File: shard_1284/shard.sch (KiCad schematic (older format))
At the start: 4 parts, among them J0 Shard, J1 ISP, U1 ATmega1284P-MU

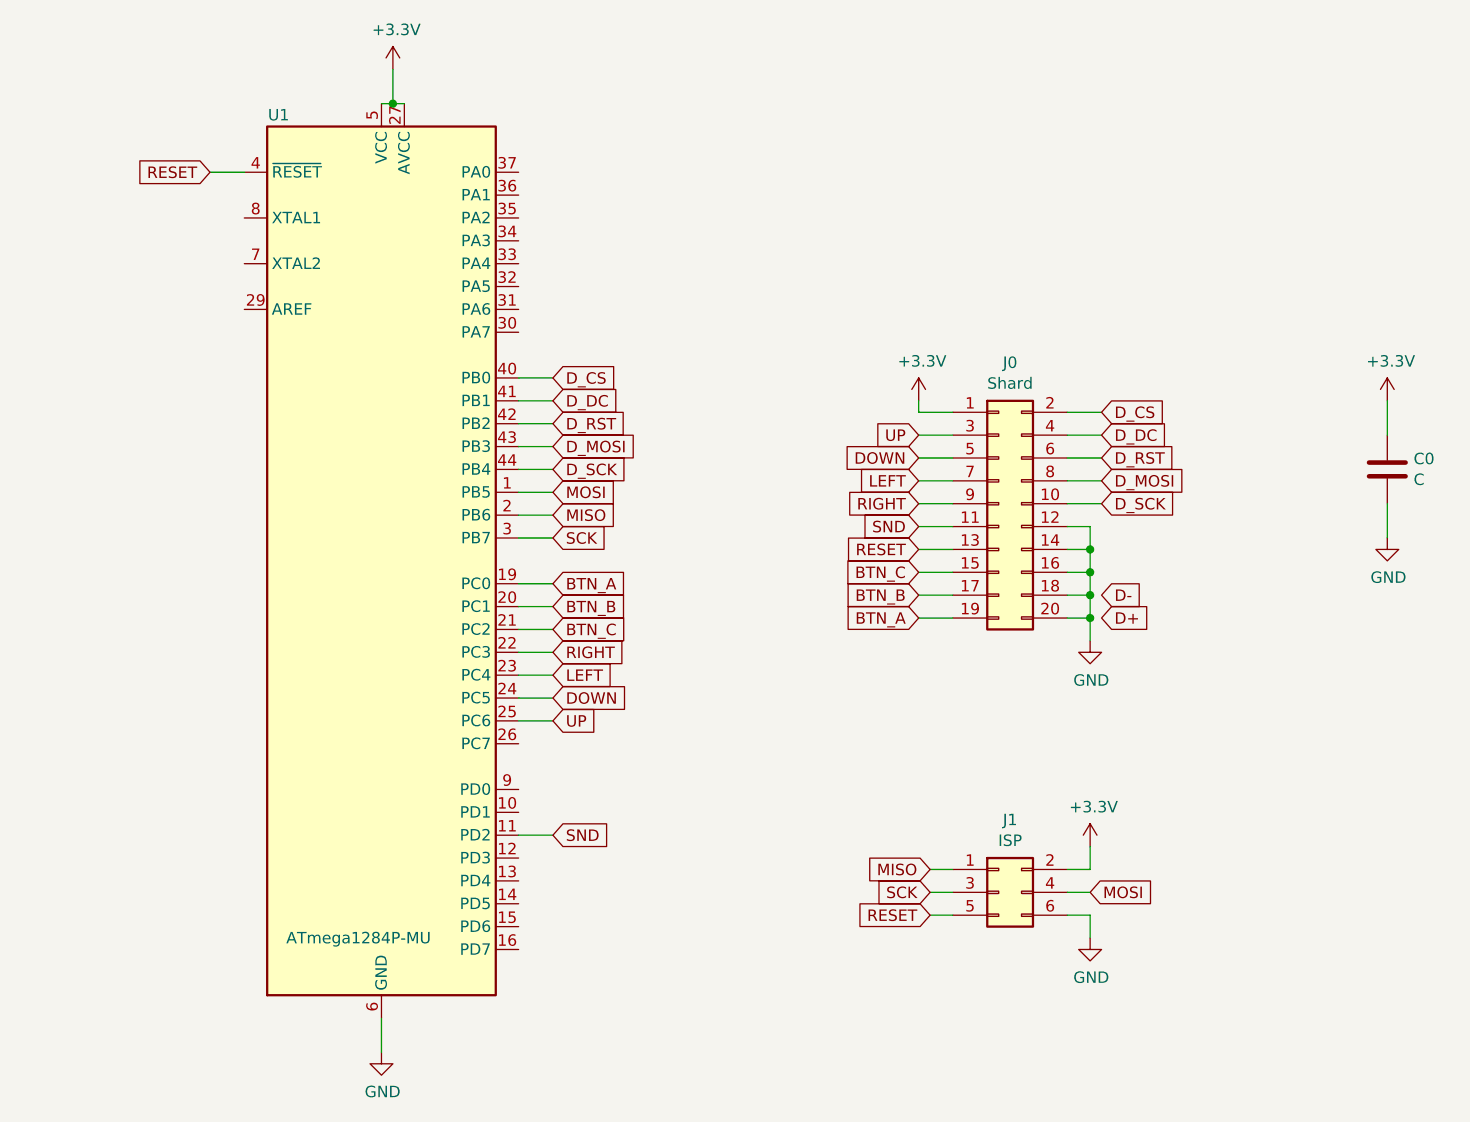
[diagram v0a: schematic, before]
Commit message: flip connector
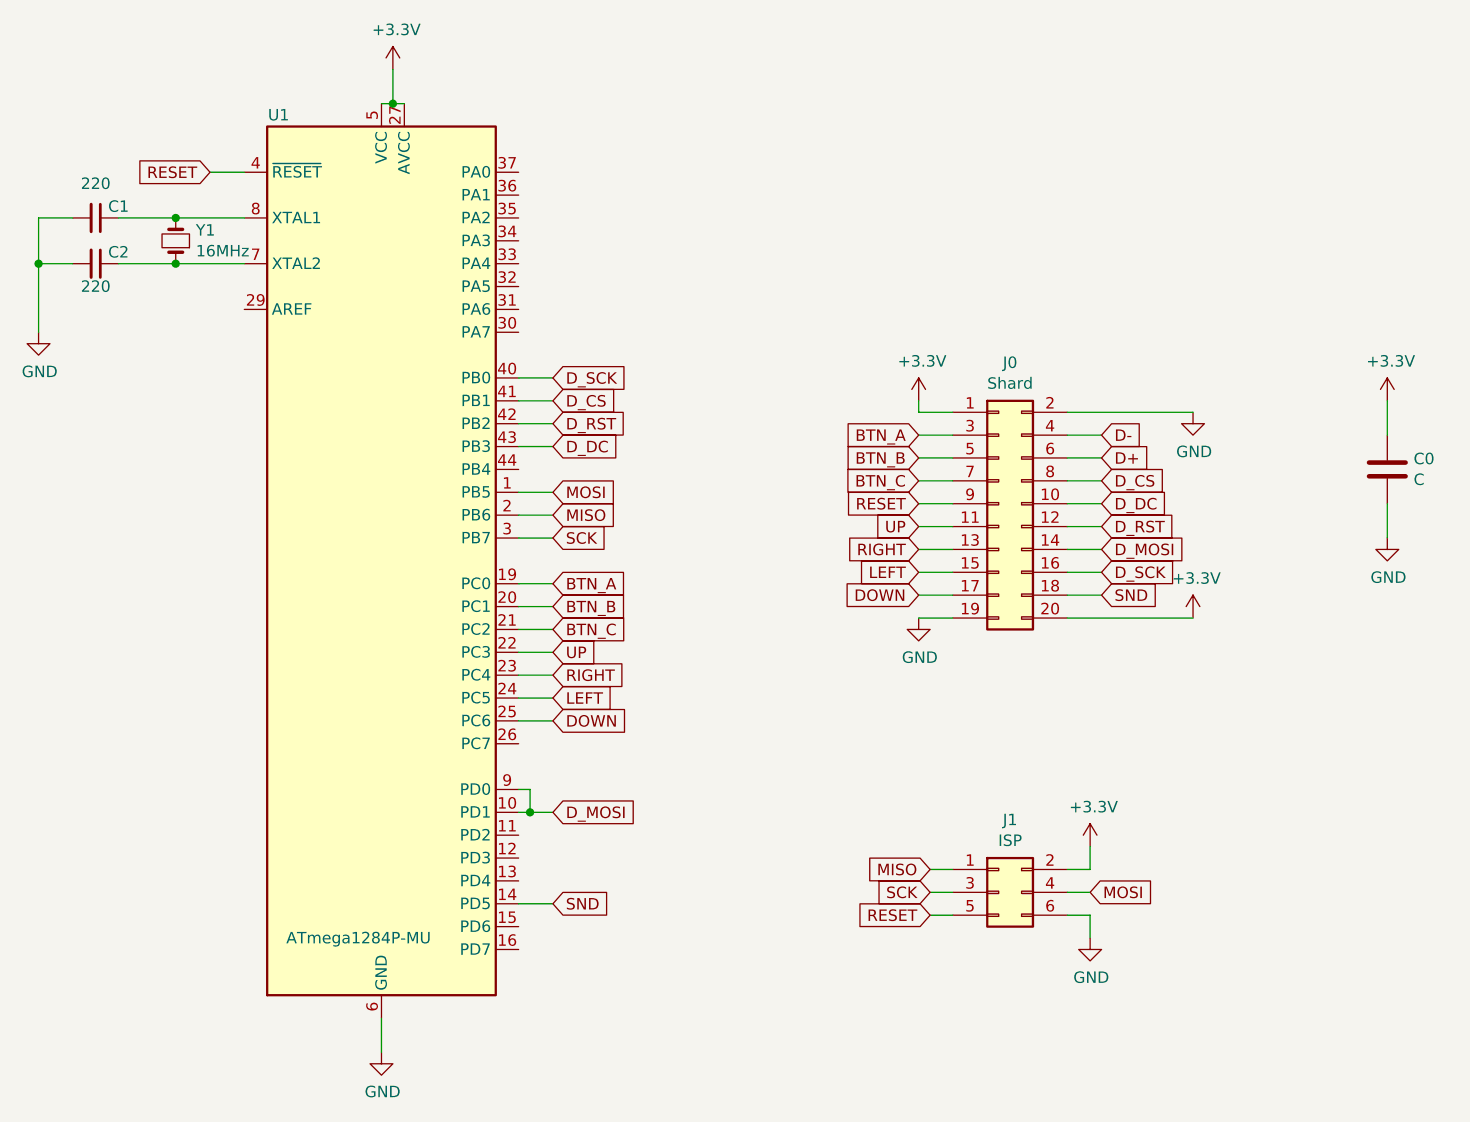
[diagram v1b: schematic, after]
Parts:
- added C1, C2: 220, Capacitor_THT:C_Rect_L7.0mm_W2.5mm_P5.00mm, symbol Device:C_Small
- added Y1: 16MHz, Crystal:Resonator-2Pin_W10.0mm_H5.0mm, symbol Device:Crystal_Small
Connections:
- net +3V3: now also J0.20 (Pin_20)
- net BTN_A: now also J0.3 (Pin_3); no longer J0.19 (Pin_19)
- net BTN_B: now also J0.5 (Pin_5); no longer J0.17 (Pin_17)
- net BTN_C: now also J0.7 (Pin_7); no longer J0.15 (Pin_15)
- net D+: now also J0.6 (Pin_6)
- net D-: now also J0.4 (Pin_4)
- net DOWN: now also J0.17 (Pin_17), U1.25 (PC6); no longer J0.5 (Pin_5), U1.24 (PC5)
- net D_CS: now also J0.8 (Pin_8), U1.41 (PB1); no longer J0.2 (Pin_2), U1.40 (PB0)
- net D_DC: now also J0.10 (Pin_10), U1.43 (PB3); no longer J0.4 (Pin_4), U1.41 (PB1)
- net D_MOSI: now also J0.14 (Pin_14), U1.10 (PD1), U1.9 (PD0); no longer J0.8 (Pin_8), U1.43 (PB3)
- net D_RST: now also J0.12 (Pin_12); no longer J0.6 (Pin_6)
- net D_SCK: now also J0.16 (Pin_16), U1.40 (PB0); no longer J0.10 (Pin_10), U1.44 (PB4)
- net GND: now also J0.19 (Pin_19), J0.2 (Pin_2), C1.2, C2.2; no longer J0.12 (Pin_12), J0.14 (Pin_14), J0.16 (Pin_16), J0.18 (Pin_18), J0.20 (Pin_20)
- net LEFT: now also J0.15 (Pin_15), U1.24 (PC5); no longer J0.7 (Pin_7), U1.23 (PC4)
- net RESET: now also J0.9 (Pin_9); no longer J0.13 (Pin_13)
- net RIGHT: now also J0.13 (Pin_13), U1.23 (PC4); no longer J0.9 (Pin_9), U1.22 (PC3)
- net SND: now also J0.18 (Pin_18), U1.14 (PD5); no longer J0.11 (Pin_11), U1.11 (PD2)
- net UP: now also J0.11 (Pin_11), U1.22 (PC3); no longer J0.3 (Pin_3), U1.25 (PC6)
- net at U1.7 (XTAL2): now also C2.1, Y1.1
- net at U1.8 (XTAL1): now also C1.1, Y1.2
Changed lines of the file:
@@
 L power:GND #PWR0102
 U 1 1 5BE69B29
-P 6500 3800
-F 0 "#PWR0102" H 6500 3550 50  0001 C CNN
-F 1 "GND" H 6505 3627 50  0000 C CNN
-F 2 "" H 6500 3800 50  0001 C CNN
-F 3 "" H 6500 3800 50  0001 C CNN
-	1    6500 3800
+P 5750 3700
+F 0 "#PWR0102" H 5750 3450 50  0001 C CNN
+F 1 "GND" H 5755 3527 50  0000 C CNN
+F 2 "" H 5750 3700 50  0001 C CNN
+F 3 "" H 5750 3700 50  0001 C CNN
+	1    5750 3700
 	1    0    0    -1
 $EndComp
@@
 $EndComp
 Wire Wire Line
-	6400 3700 6500 3700
-Wire Wire Line
-	6500 3700 6500 3800
-Wire Wire Line
-	6400 3600 6500 3600
-Wire Wire Line
-	6500 3600 6500 3700
-Connection ~ 6500 3700
-Wire Wire Line
-	6400 3500 6500 3500
-Wire Wire Line
-	6500 3500 6500 3600
-Connection ~ 6500 3600
-Wire Wire Line
-	6400 3400 6500 3400
-Wire Wire Line
-	6500 3400 6500 3500
-Connection ~ 6500 3500
-Wire Wire Line
-	6400 3300 6500 3300
-Wire Wire Line
-	6500 3300 6500 3400
-Connection ~ 6500 3400
-Wire Wire Line
 	5750 2750 5750 2800
 Wire Wire Line
 	5750 2800 5900 2800
-Text GLabel 6550 2800 2    50   Input ~ 0
+Text GLabel 6550 3100 2    50   Input ~ 0
 D_CS
-Text GLabel 6550 2900 2    50   Input ~ 0
+Text GLabel 6550 3200 2    50   Input ~ 0
 D_DC
-Text GLabel 6550 3000 2    50   Input ~ 0
+Text GLabel 6550 3300 2    50   Input ~ 0
 D_RST
-Text GLabel 6550 3100 2    50   Input ~ 0
+Text GLabel 6550 3400 2    50   Input ~ 0
 D_MOSI
-Text GLabel 6550 3200 2    50   Input ~ 0
+Text GLabel 6550 3500 2    50   Input ~ 0
 D_SCK
 Wire Wire Line
-	6400 2800 6550 2800
-Wire Wire Line
 	6400 2900 6550 2900
 Wire Wire Line
@@
 Wire Wire Line
 	6400 3200 6550 3200
+Text GLabel 5750 3300 0    50   Input ~ 0
+UP
+Text GLabel 5750 3600 0    50   Input ~ 0
+DOWN
+Text GLabel 5750 3500 0    50   Input ~ 0
+LEFT
+Text GLabel 5750 3400 0    50   Input ~ 0
+RIGHT
+Text GLabel 6550 3600 2    50   Input ~ 0
+SND
+Text GLabel 5750 3200 0    50   Input ~ 0
+RESET
+Text GLabel 5750 3100 0    50   Input ~ 0
+BTN_C
+Text GLabel 5750 3000 0    50   Input ~ 0
+BTN_B
 Text GLabel 5750 2900 0    50   Input ~ 0
-UP
-Text GLabel 5750 3000 0    50   Input ~ 0
-DOWN
-Text GLabel 5750 3100 0    50   Input ~ 0
-LEFT
-Text GLabel 5750 3200 0    50   Input ~ 0
-RIGHT
-Text GLabel 5750 3300 0    50   Input ~ 0
-SND
-Text GLabel 5750 3400 0    50   Input ~ 0
-RESET
-Text GLabel 5750 3500 0    50   Input ~ 0
-BTN_C
-Text GLabel 5750 3600 0    50   Input ~ 0
-BTN_B
-Text GLabel 5750 3700 0    50   Input ~ 0
 BTN_A
 Wire Wire Line
@@
 Wire Wire Line
 	7800 3200 7800 3350
-Text GLabel 6550 3700 2    50   Input ~ 0
+Text GLabel 6550 3000 2    50   Input ~ 0
 D+
-Text GLabel 6550 3600 2    50   Input ~ 0
+Text GLabel 6550 2900 2    50   Input ~ 0
 D-
 $Comp
@@
 	1    0    0    -1
 $EndComp
+Text GLabel 4150 3850 2    50   Input ~ 0
+UP
 Text GLabel 4150 4150 2    50   Input ~ 0
-UP
+DOWN
 Text GLabel 4150 4050 2    50   Input ~ 0
-DOWN
+LEFT
 Text GLabel 4150 3950 2    50   Input ~ 0
-LEFT
-Text GLabel 4150 3850 2    50   Input ~ 0
 RIGHT
 Text GLabel 4150 3750 2    50   Input ~ 0
@@
 Text GLabel 4150 3550 2    50   Input ~ 0
 BTN_A
-Text GLabel 4150 2650 2    50   Input ~ 0
+Text GLabel 4150 2750 2    50   Input ~ 0
 D_CS
-Text GLabel 4150 2750 2    50   Input ~ 0
+Text GLabel 4150 2950 2    50   Input ~ 0
 D_DC
 Text GLabel 4150 2850 2    50   Input ~ 0
 D_RST
-Text GLabel 4150 2950 2    50   Input ~ 0
+Text GLabel 4150 4550 2    50   Input ~ 0
 D_MOSI
-Text GLabel 4150 3050 2    50   Input ~ 0
+Text GLabel 4150 2650 2    50   Input ~ 0
 D_SCK
 $Comp
@@
 	4000 2950 4150 2950
 Wire Wire Line
-	4000 3050 4150 3050
-Wire Wire Line
 	4000 3150 4150 3150
 Wire Wire Line
@@
 Wire Wire Line
 	4000 4150 4150 4150
-Text GLabel 4150 4650 2    50   Input ~ 0
+Text GLabel 4150 4950 2    50   Input ~ 0
 SND
-Wire Wire Line
-	4000 4650 4150 4650
+$Comp
+L power:GND #PWR02
+U 1 1 5BEC77E8
+P 6950 2800
+F 0 "#PWR02" H 6950 2550 50  0001 C CNN
+F 1 "GND" H 6955 2627 50  0000 C CNN
+F 2 "" H 6950 2800 50  0001 C CNN
+F 3 "" H 6950 2800 50  0001 C CNN
+	1    6950 2800
+	1    0    0    -1
+$EndComp
+$Comp
+L power:+3.3V #PWR03
+U 1 1 5BEC7B87
+P 6950 3700
+F 0 "#PWR03" H 6950 3550 50  0001 C CNN
+F 1 "+3.3V" H 6965 3873 50  0000 C CNN
+F 2 "" H 6950 3700 50  0001 C CNN
+F 3 "" H 6950 3700 50  0001 C CNN
+	1    6950 3700
+	1    0    0    -1
+$EndComp
+Wire Wire Line
+	6400 3700 6950 3700
+Wire Wire Line
+	6400 2800 6950 2800
+Wire Wire Line
+	6400 3300 6550 3300
+Wire Wire Line
+	6400 3400 6550 3400
+Wire Wire Line
+	6550 3500 6400 3500
+Wire Wire Line
+	6400 3600 6550 3600
+$Comp
+L Device:Crystal_Small Y1
+U 1 1 5BECE84F
+P 2500 2050
+F 0 "Y1" V 2546 1962 50  0000 R CNN
+F 1 "16MHz" V 2455 1962 50  0000 R CNN
+F 2 "Crystal:Resonator-2Pin_W10.0mm_H5.0mm" H 2500 2050 50  0001 C CNN
+F 3 "~" H 2500 2050 50  0001 C CNN
+	1    2500 2050
+	0    -1   -1   0
+$EndComp
+Wire Wire Line
+	2800 2150 2500 2150
+Wire Wire Line
+	2500 1950 2800 1950
+$Comp
+L power:GND #PWR01
+U 1 1 5BED1155
+P 1900 2450
+F 0 "#PWR01" H 1900 2200 50  0001 C CNN
+F 1 "GND" H 1905 2277 50  0000 C CNN
+F 2 "" H 1900 2450 50  0001 C CNN
+F 3 "" H 1900 2450 50  0001 C CNN
+	1    1900 2450
+	1    0    0    -1
+$EndComp
+$Comp
+L Device:C_Small C1
+U 1 1 5BED1404
+P 2150 1950
+F 0 "C1" V 2100 2050 50  0000 C CNN
+F 1 "220" V 2000 1950 50  0000 C CNN
+F 2 "Capacitor_THT:C_Rect_L7.0mm_W2.5mm_P5.00mm" H 2150 1950 50  0001 C CNN
+F 3 "~" H 2150 1950 50  0001 C CNN
+	1    2150 1950
+	0    1    1    0
+$EndComp
+$Comp
+L Device:C_Small C2
+U 1 1 5BED1562
+P 2150 2150
+F 0 "C2" V 2100 2250 50  0000 C CNN
+F 1 "220" V 2250 2150 50  0000 C CNN
+F 2 "Capacitor_THT:C_Rect_L7.0mm_W2.5mm_P5.00mm" H 2150 2150 50  0001 C CNN
+F 3 "~" H 2150 2150 50  0001 C CNN
+	1    2150 2150
+	0    1    1    0
+$EndComp
+Wire Wire Line
+	2500 1950 2250 1950
+Connection ~ 2500 1950
+Wire Wire Line
+	2500 2150 2250 2150
+Connection ~ 2500 2150
+Wire Wire Line
+	2050 1950 1900 1950
+Wire Wire Line
+	1900 1950 1900 2150
+Wire Wire Line
+	2050 2150 1900 2150
+Connection ~ 1900 2150
+Wire Wire Line
+	1900 2150 1900 2450
+Wire Wire Line
+	4000 4950 4150 4950
+Wire Wire Line
+	4000 4450 4050 4450
+Wire Wire Line
+	4050 4550 4150 4550
+Wire Wire Line
+	4000 4550 4050 4550
+Connection ~ 4050 4550
+Wire Wire Line
+	4050 4450 4050 4550
 $EndSCHEMATC
